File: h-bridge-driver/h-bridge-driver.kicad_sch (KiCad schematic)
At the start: 20 parts

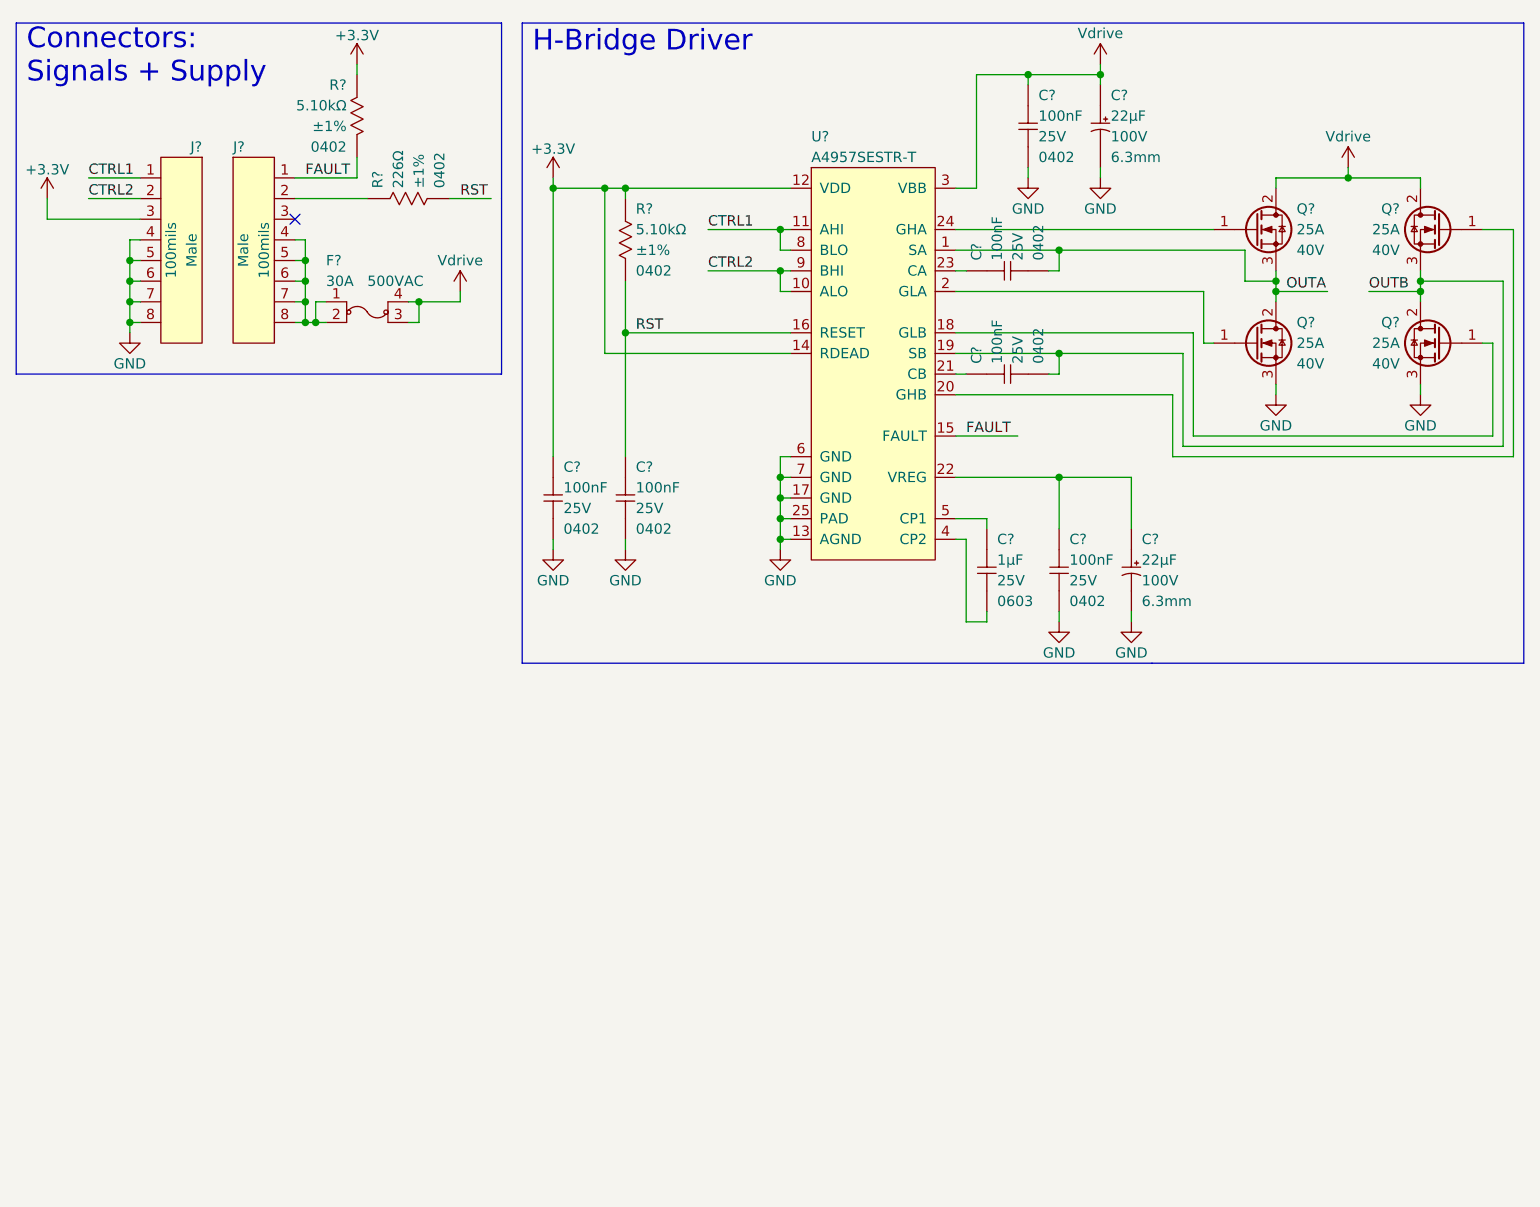
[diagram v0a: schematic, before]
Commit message: Complete H bridge driver
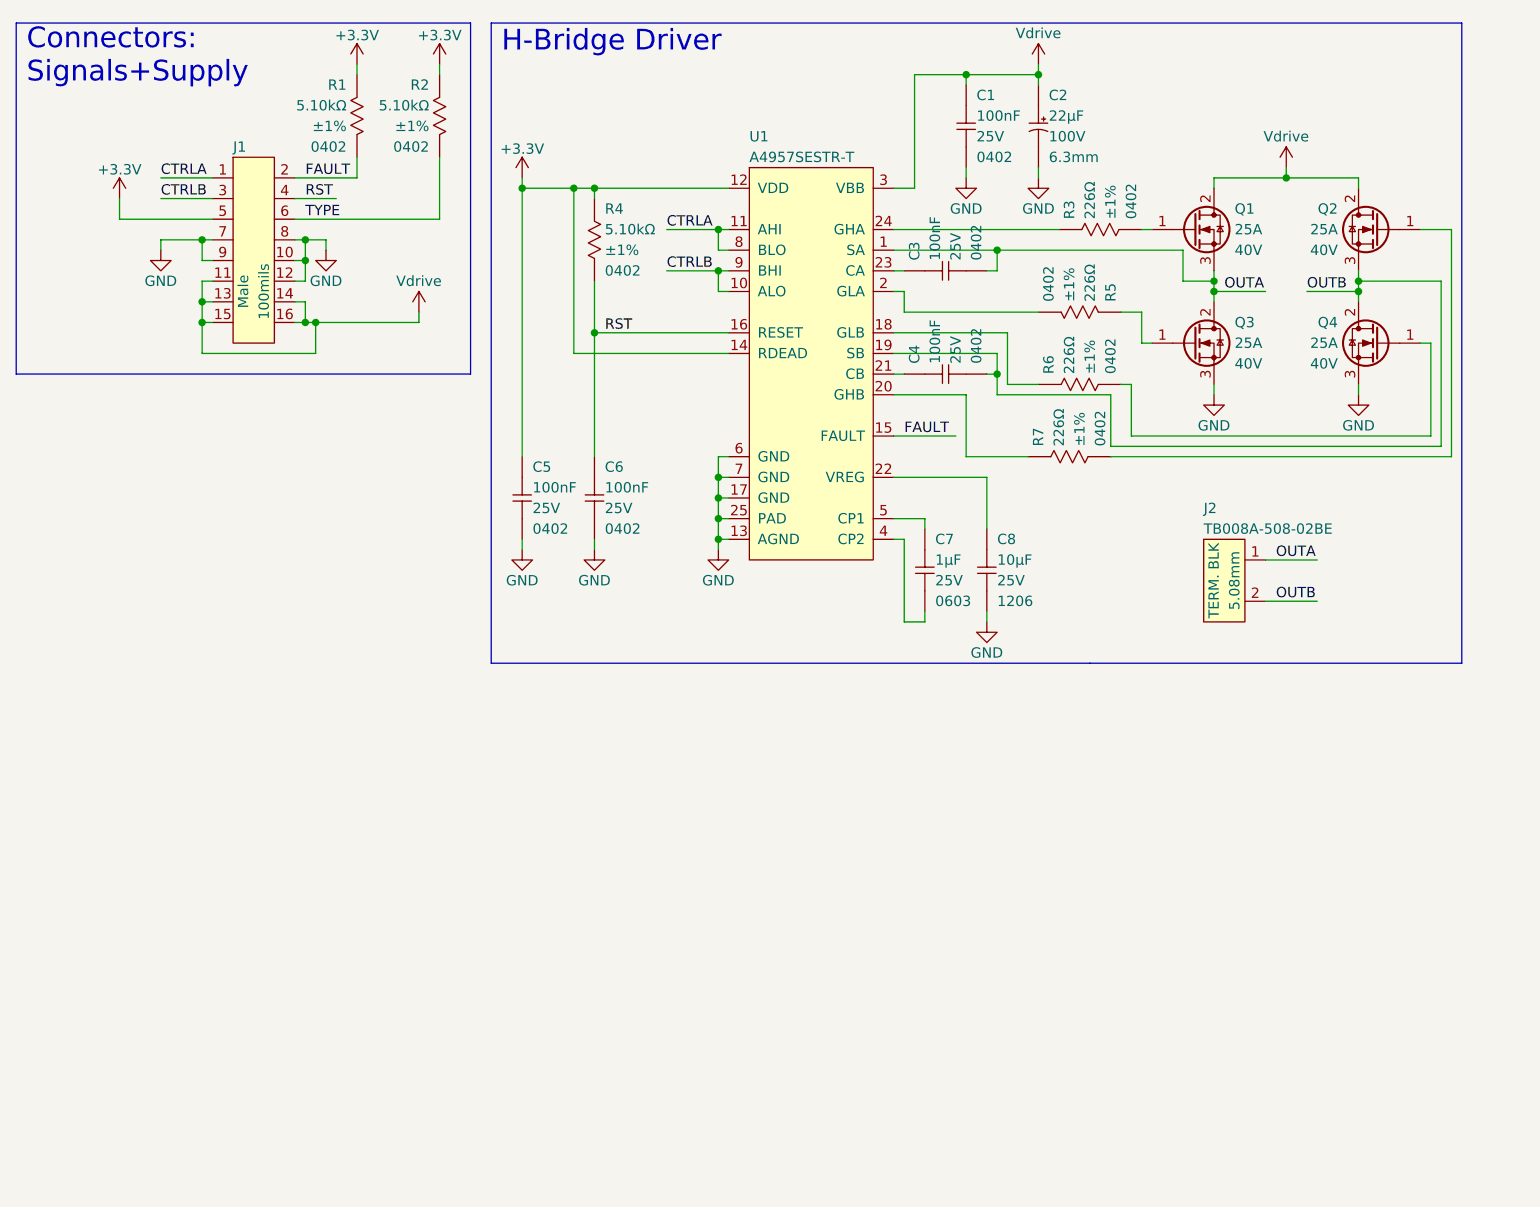
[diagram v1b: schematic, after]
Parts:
- removed C?: CAP_CER_100NF_25V_0402, connaxio-capacitors:CAP_CER_0402_1005M, symbol connaxio-capacitors:CAP_CER_100NF_25V_0402
- removed C?: CAP_AE_22UF_100V_TH_6.3MM, connaxio-capacitors:CAP_AE_RAD_D6.3_H12.5_P2.5, symbol connaxio-capacitors:CAP_AE_22UF_100V_TH_6.3MM
- removed F?: FUS_BLADE_3522, connaxio-connectors:FUS_BLADE_3522, symbol connaxio-connectors:FUS_BLADE_3522
- removed J? (x2): CON_HDR_100MILS_M_TH_1X8, connaxio-connectors:CON_HDR_100MILS_M_TH_1X8, symbol connaxio-connectors:CON_HDR_100MILS_M_TH_1X8
- removed R?: RES_226Ω_1%_0402, connaxio-resistors:RES_0402_1005M, symbol connaxio-resistors:RES_226Ω_1%_0402
- added C8: CAP_CER_10UF_25V_1206, connaxio-capacitors:CAP_CER_1206_3216M, symbol connaxio-capacitors:CAP_CER_10UF_25V_1206
- added J1: CON_HDR_100MILS_M_TH_2X8, connaxio-connectors:CON_HDR_100MILS_M_TH_2X8, symbol connaxio-connectors:CON_HDR_100MILS_M_TH_2X8
- added J2: CON_TERM_BLK_1X2_TB008A-508-02BE, connaxio-connectors:CON_TERM_BLK_1X2_TB008A-508-02BE, symbol connaxio-connectors:CON_TERM_BLK_1X2_TB008A-508-02BE
- added R2: RES_5.10KΩ_1%_0402, connaxio-resistors:RES_0402_1005M, symbol connaxio-resistors:RES_5.10KΩ_1%_0402
- added R3, R5, R6, R7: RES_226Ω_1%_0402, connaxio-resistors:RES_0402_1005M, symbol connaxio-resistors:RES_226Ω_1%_0402
- gave numbers to parts that had none: 14
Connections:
- net +3.3V: now also J1.5, R2.1
- net FAULT: now also J1.2
- net GND: now also C8.2, J1.10, J1.12, J1.7, J1.8, J1.9
- net OUTA: now also J2.1
- net OUTB: now also J2.2
- net RST: now also J1.4
- net Vdrive: now also J1.11, J1.13, J1.14, J1.15, J1.16
- net at Q3.1 (G): now also R5.1; no longer U1.2 (GLA)
- net at Q4.1 (G): now also R6.2; no longer U1.18 (GLB)
- net at U1.22 (VREG): now also C8.1
- net at Q2.1 (G): now also R7.2; no longer U1.20 (GHB)
- net at U1.24 (GHA): now also R3.1; no longer Q1.1 (G)
- net CTRL1 renamed CTRLA
- net CTRLA: now also J1.1
- net CTRL2 renamed CTRLB
- net CTRLB: now also J1.3
- new net: R6.1, U1.18 (GLB)
- new net: R5.2, U1.2 (GLA)
- new net: R7.1, U1.20 (GHB)
- new net: Q1.1 (G), R3.2
- new net TYPE: J1.6, R2.2
- no-connect marks 1 -> 0
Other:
- note added: "Connectors: Signals+Supply"
- note removed: "Connectors: Signals + Supply"
- moved on the sheet: C1, C2, C3, C4, C5, C6, C7, Q1, Q2, Q3, Q4, R4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

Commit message: Add IO expanders, add simple PMOS switch, add 5V TVS,
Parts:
- removed R1, R2: RES_5.10KΩ_1%_0402, connaxio-resistors:RES_0402_1005M, symbol connaxio-resistors:RES_5.10KΩ_1%_0402
- renumbered R3 to R1, R4 to R2, R5 to R3, R6 to R4, R7 to R5
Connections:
- net TYPE: no longer names the net of J1.6
- no-connect marks 0 -> 1

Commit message: Add motor driver page and I2C proteciton adapter, current & temp sensor
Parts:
- added F1, F2, F3, F4: FID_1X1, connaxio-mechanical:FID_1X1, symbol connaxio-mechanical:FID_1X1
- renumbered C5 to C1, C6 to C2, C7 to C3, C3 to C4, C4 to C5, C1 to C6, C8 to C7, C2 to C8, Q3 to Q2, Q2 to Q3, R2 to R1, R5 to R2, R1 to R5
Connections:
- net GND: now also F1.1, F2.1
- net Vdrive: now also F3.1, F4.1
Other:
- note added: "Connector: Signals+Supply"
- note added: "Fiducials"
- note removed: "Connectors: Signals+Supply"
- moved on the sheet: C1, C2, C3, C4, C5, C6, C7, C8, J2, Q1, Q2, Q3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

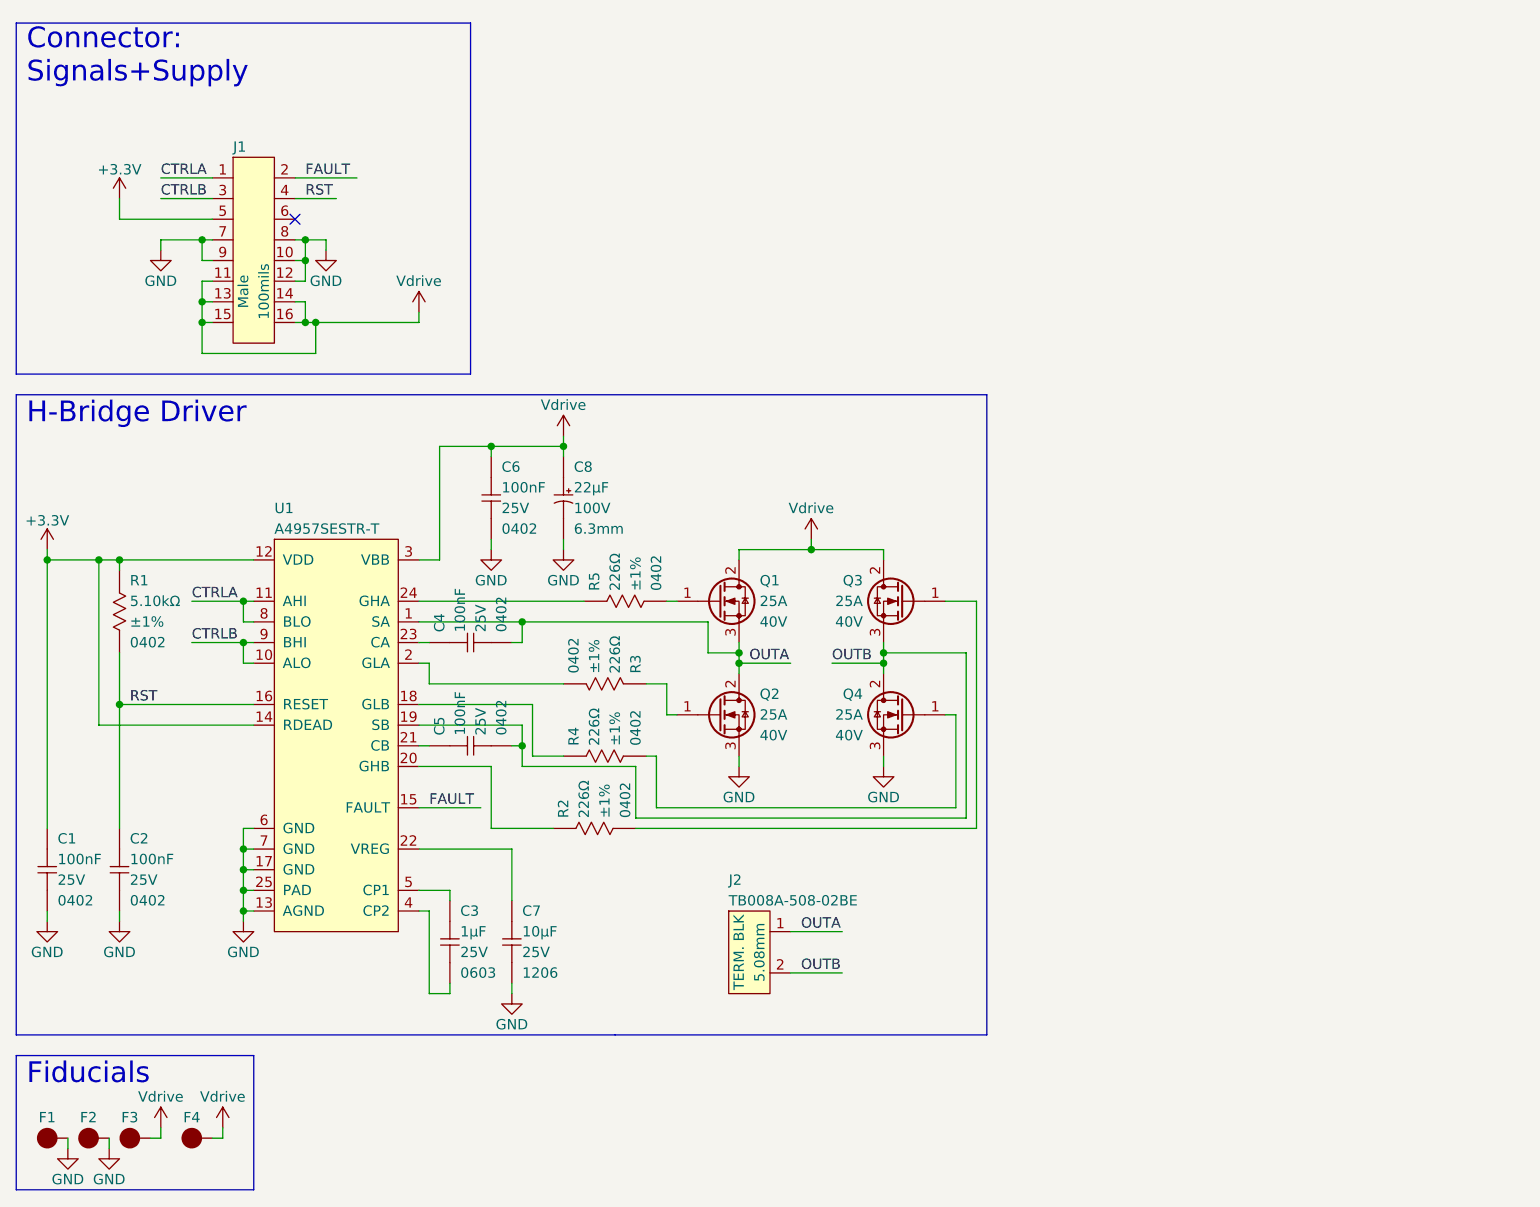
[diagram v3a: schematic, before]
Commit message: Move fuse to motor driver board Optimize board array schematic (hierarchical schematics)
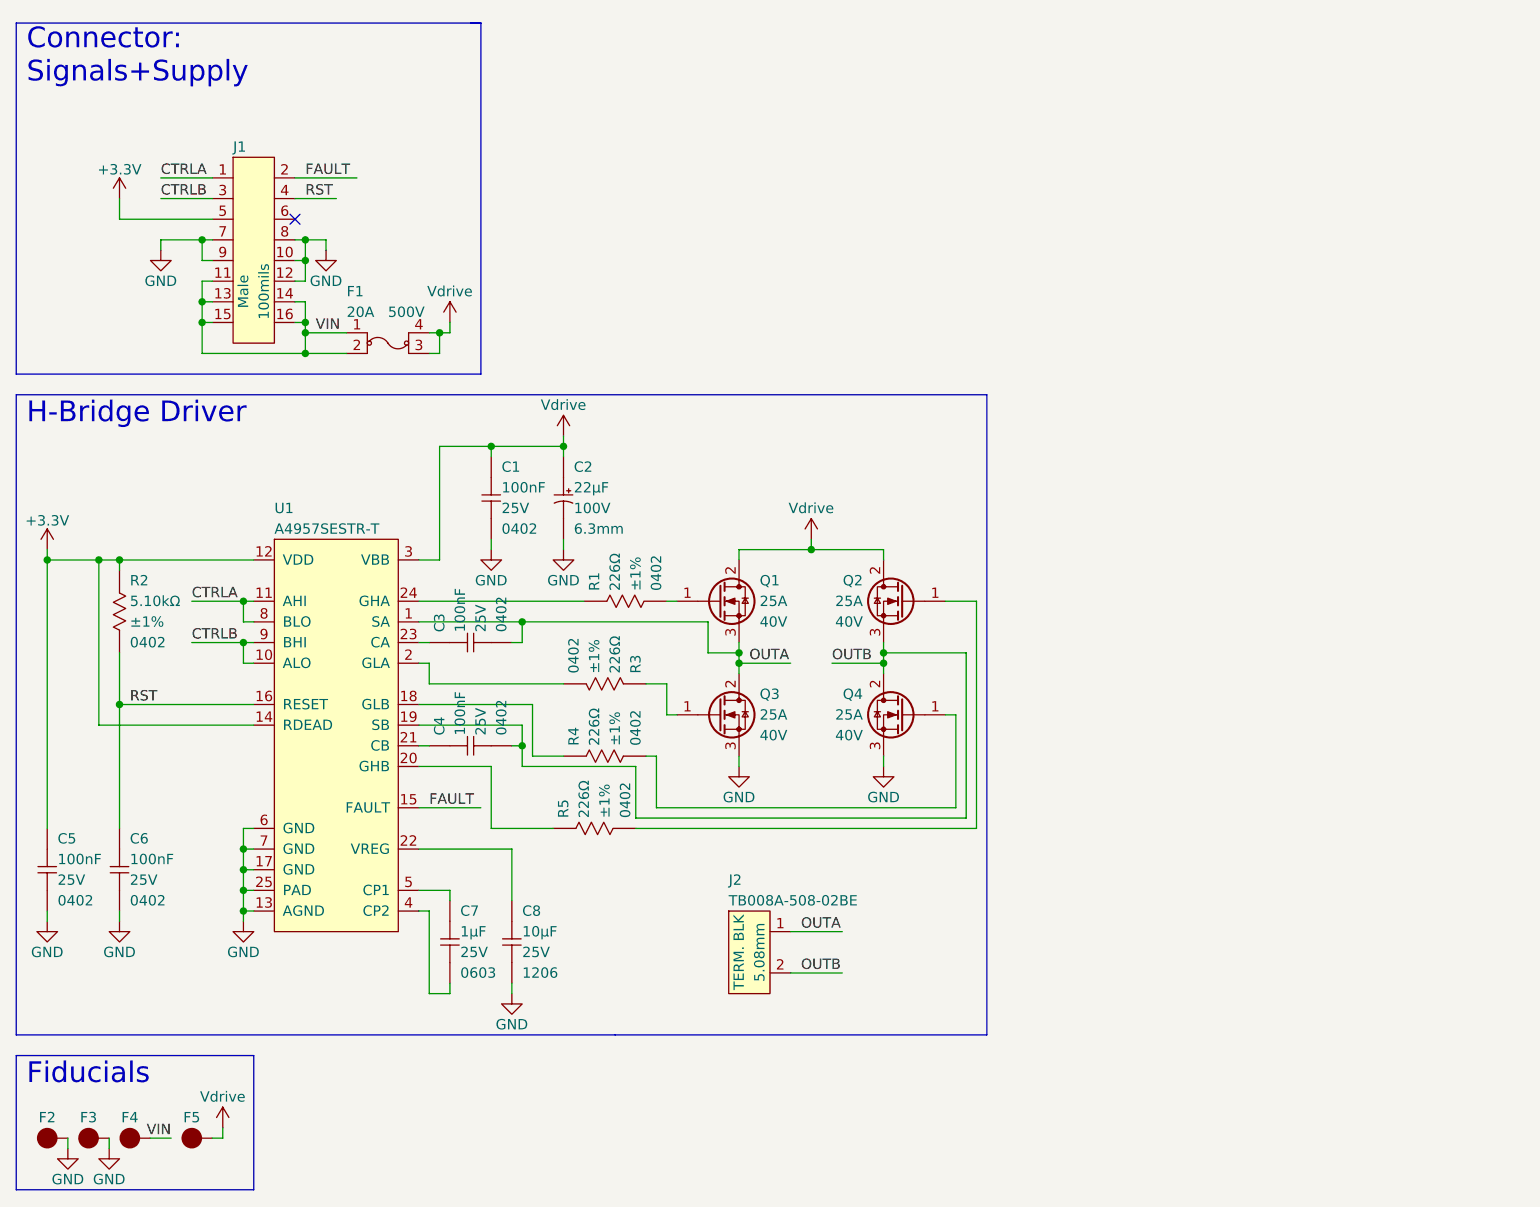
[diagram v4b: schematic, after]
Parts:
- added F1: FUS_BLADE_MINI_3588-1, connaxio-connectors:FUS_BLADE_MINI_3588-1, symbol connaxio-connectors:FUS_BLADE_MINI_3588-1
- renumbered C6 to C1, C8 to C2, C4 to C3, C5 to C4, C1 to C5, C2 to C6, C3 to C7, C7 to C8, F1 to F2, F2 to F3, F3 to F4, F4 to F5, Q3 to Q2, Q2 to Q3, R5 to R1, R1 to R2, R2 to R5
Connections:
- net Vdrive: now also F1.3, F1.4; no longer F4.1, J1.11, J1.13, J1.14, J1.15, J1.16
- new net VIN: F1.1, F1.2, F4.1, J1.11, J1.13, J1.14, J1.15, J1.16
